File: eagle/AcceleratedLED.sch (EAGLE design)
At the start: 33 parts, among them IC1 TPS62133, Q1 16MHZ, U1 ATMEGA328, U6 SPX3819, U8 TXB0108PWR

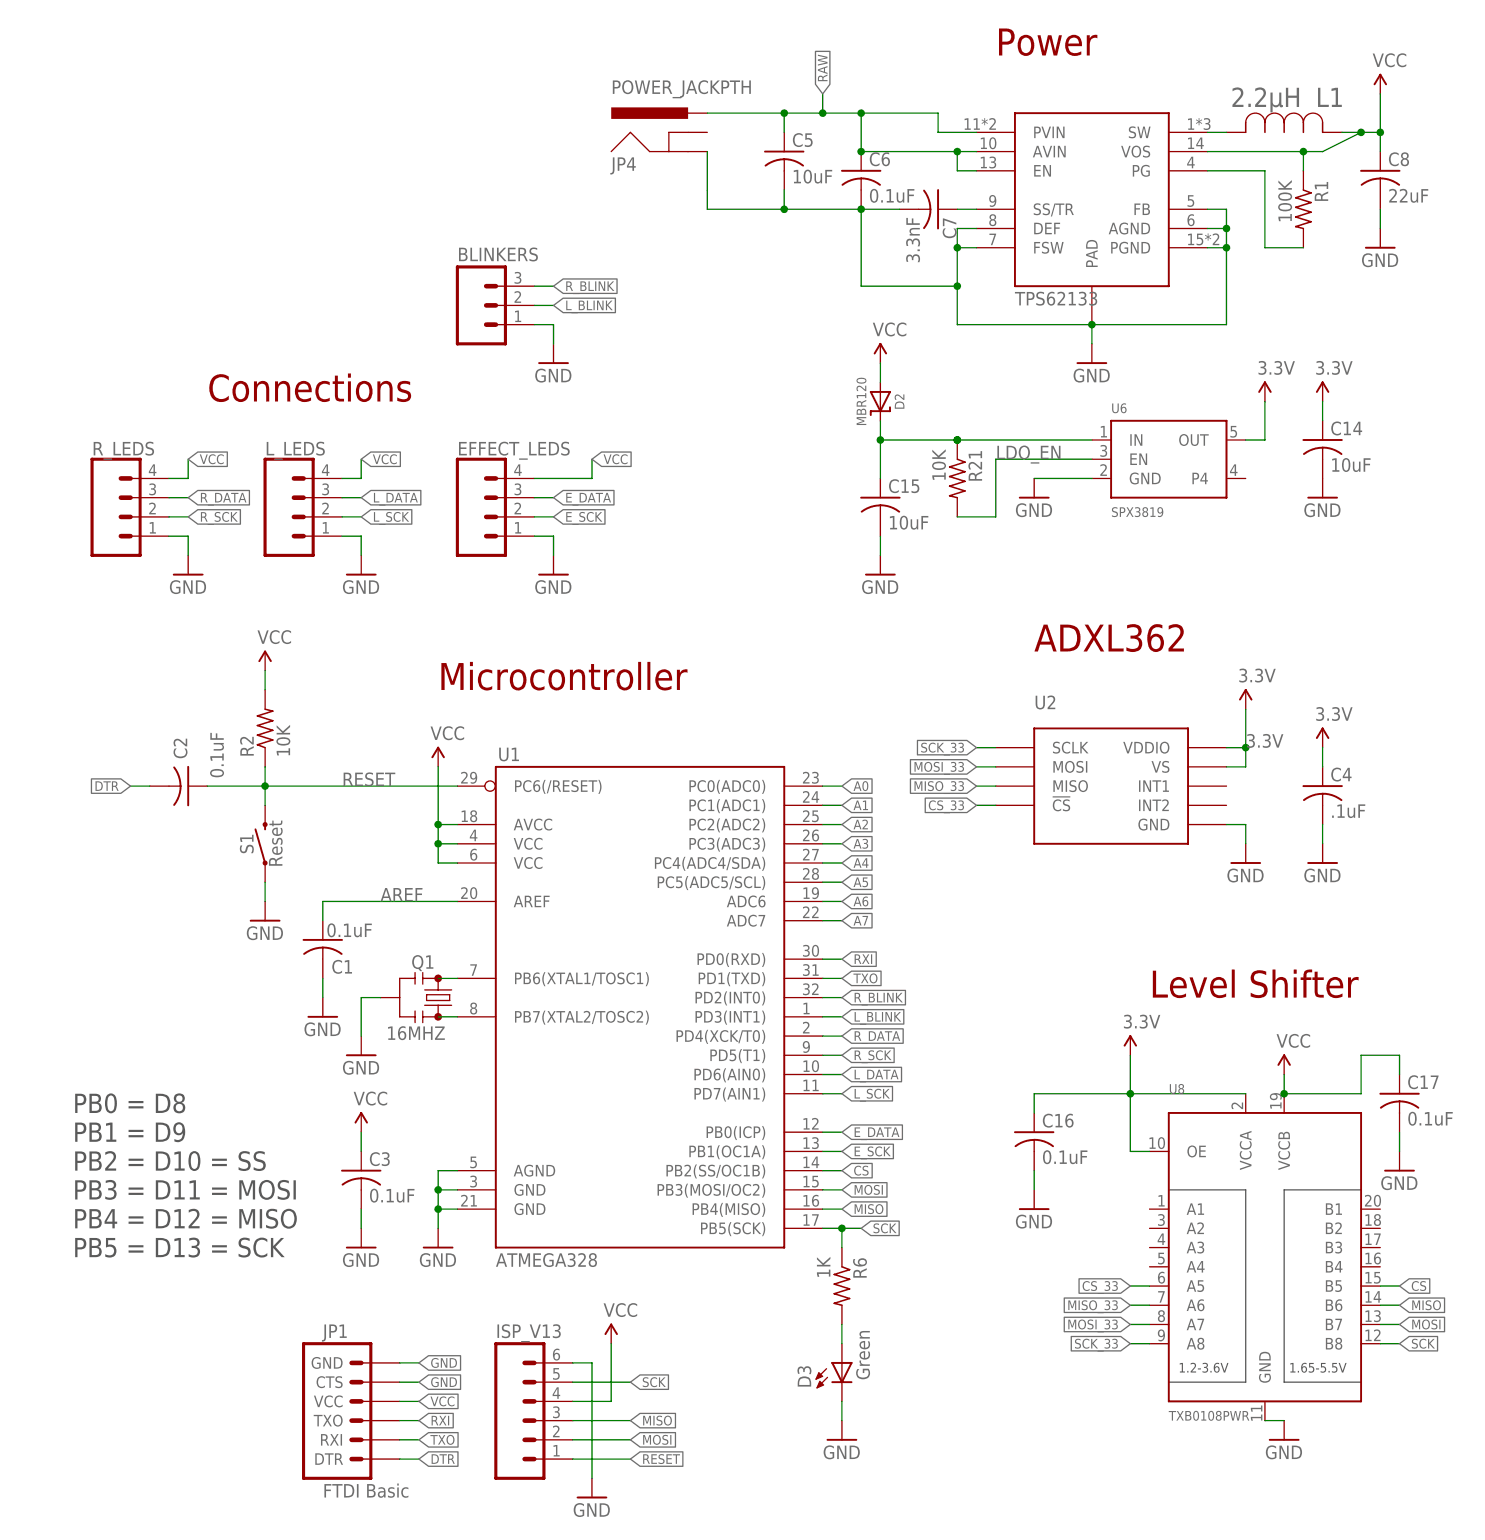
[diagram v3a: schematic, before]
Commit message: Move to support R1,L1,R2,L2 strands
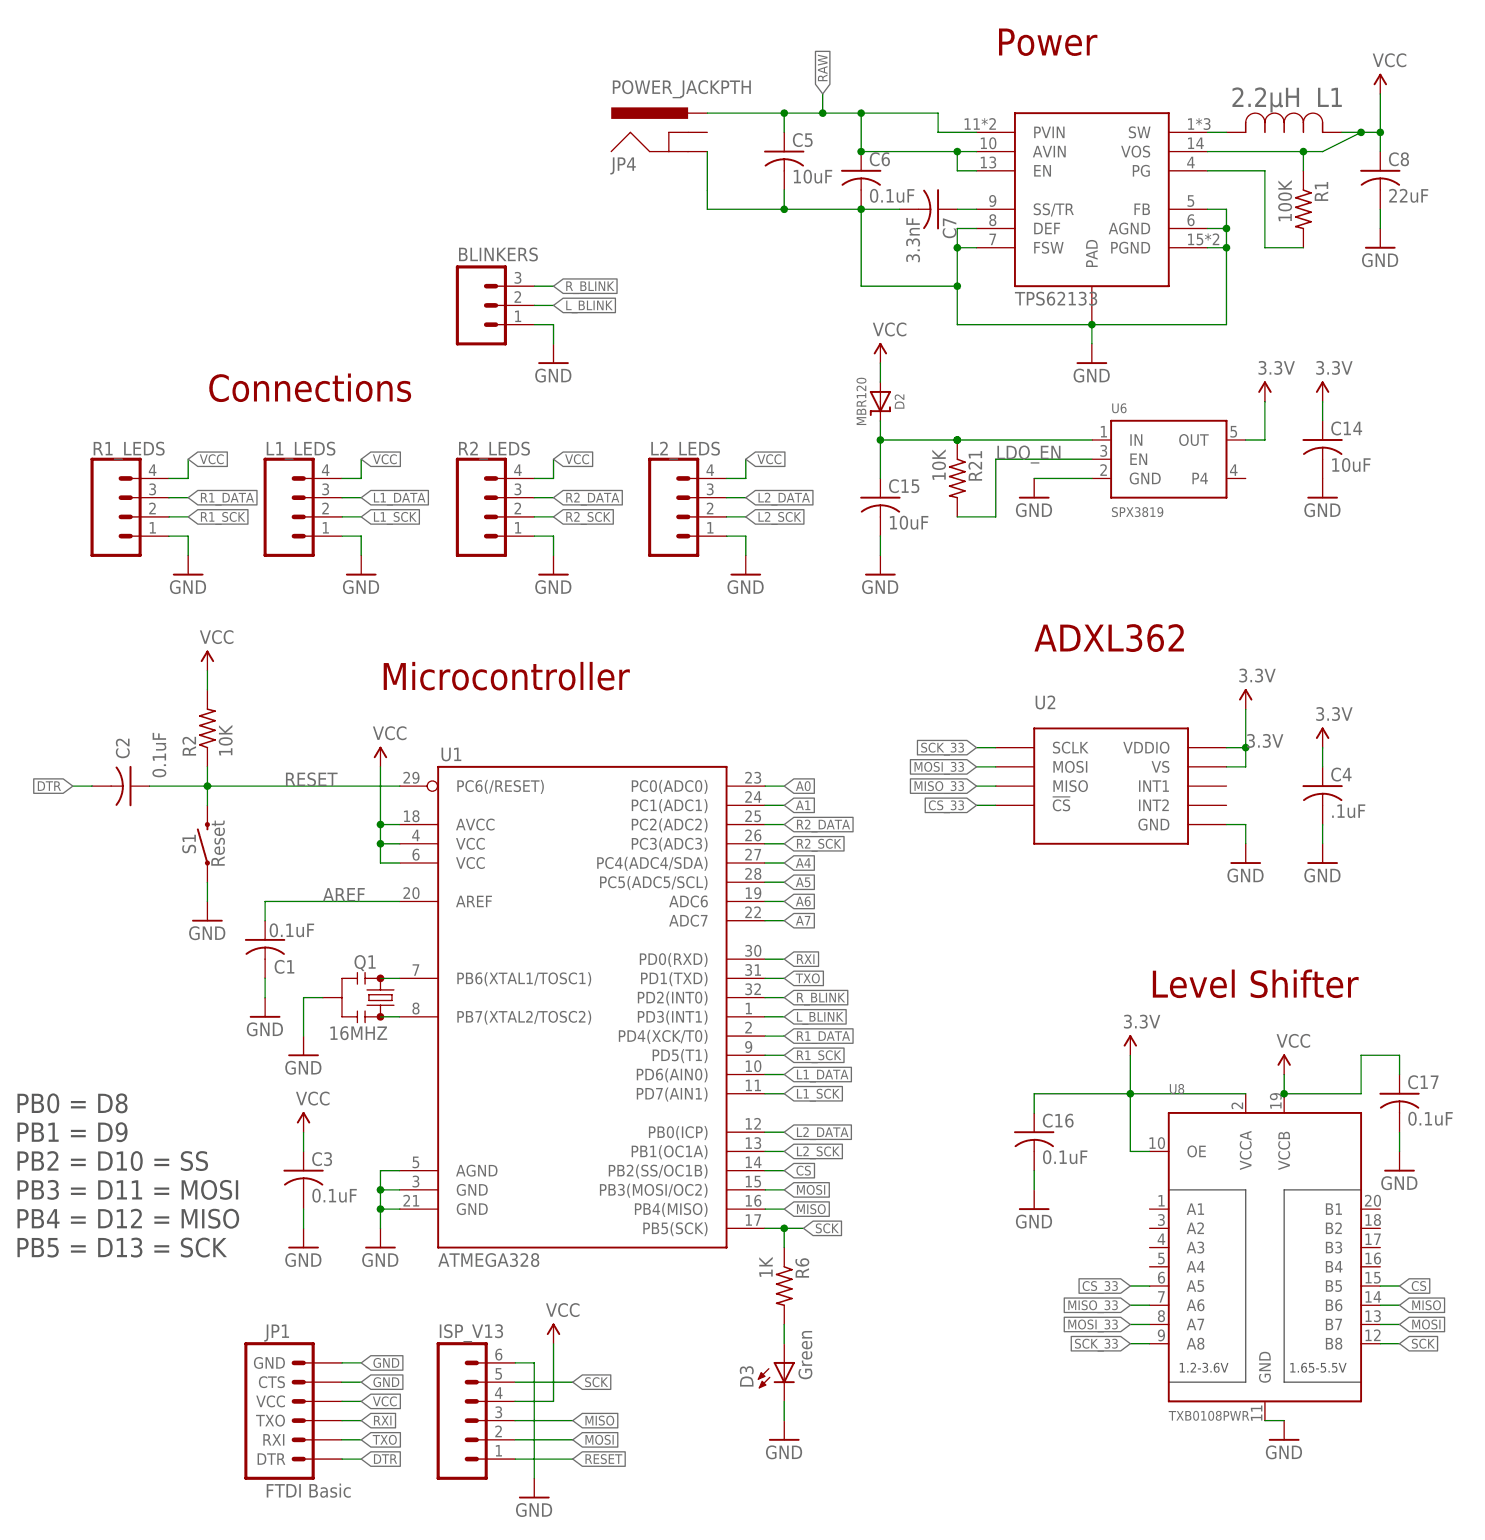
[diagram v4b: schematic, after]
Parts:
- added L2_LEDS: (no value), MotionSign:CONN_04JST-PTH
- renumbered EFFECT_LEDS to R2_LEDS, L_LEDS to L1_LEDS, R_LEDS to R1_LEDS
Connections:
- net L_DATA renamed L1_DATA
- net L_SCK renamed L1_SCK
- net R_DATA renamed R1_DATA
- net R_SCK renamed R1_SCK
- removed net A2: U1.PC2(ADC2)
- removed net A3: U1.PC3(ADC3)
- removed net E_DATA: R2_LEDS.3, U1.PB0(ICP)
- removed net E_SCK: R2_LEDS.2, U1.PB1(OC1A)
- new net L2_DATA: L2_LEDS.3, U1.PB0(ICP)
- new net L2_SCK: L2_LEDS.2, U1.PB1(OC1A)
- new net R2_DATA: R2_LEDS.3, U1.PC2(ADC2)
- new net R2_SCK: R2_LEDS.2, U1.PC3(ADC3)
- net GND: now also L2_LEDS.1
- net VCC: now also L2_LEDS.4
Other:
- moved on the sheet: C1, C2, C3, D3, ISP_V13, JP1, Q1, R2, R6, S1, U1
